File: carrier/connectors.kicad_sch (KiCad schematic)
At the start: 12 parts, among them J1 USB_C_Receptacle_USB2.0, J4 HDMI_D_1.4, J5 USB_C_Receptacle_USB2.0

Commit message: pcb
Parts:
- removed R15: 0, Resistor_SMD:R_0603_1608Metric_Pad0.98x0.95mm_HandSolder, symbol Device:R
- removed R58: 0, Resistor_SMD:R_1210_3225Metric_Pad1.30x2.65mm_HandSolder, symbol Device:R
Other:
- note removed: "Too many people on stack overflow/exchange seem to be unable to agree on this! Leaving this unconnected with a 0 ohm so we can if we choose to - but grounding it could apparently cause a ground loop thingy (which would probably happen since we do not have a true ground in batterys i guess?)"
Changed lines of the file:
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@@
   (junction (at 253.365 46.355) (diameter 0.9144) (color 0 0 0 0))
   (junction (at 271.145 121.92) (diameter 0.9144) (color 0 0 0 0))
-  (junction (at 276.225 72.39) (diameter 0.9144) (color 0 0 0 0))
-  (junction (at 281.94 149.225) (diameter 0.9144) (color 0 0 0 0))
   (no_connect (at 36.83 28.575))
   (no_connect (at 36.83 31.115))
@@
     (stroke (width 0) (type solid) (color 0 0 0 0))
   )
-  (wire (pts (xy 273.685 72.39) (xy 276.225 72.39))
-    (stroke (width 0) (type solid) (color 0 0 0 0))
-  )
   (wire (pts (xy 274.32 28.575) (xy 273.05 28.575))
     (stroke (width 0) (type solid) (color 0 0 0 0))
@@
     (stroke (width 0) (type solid) (color 0 0 0 0))
   )
-  (wire (pts (xy 276.225 64.77) (xy 276.225 72.39))
-    (stroke (width 0) (type solid) (color 0 0 0 0))
-  )
-  (wire (pts (xy 276.225 72.39) (xy 276.225 73.66))
+  (wire (pts (xy 276.225 64.77) (xy 276.225 73.66))
     (stroke (width 0) (type solid) (color 0 0 0 0))
   )
@@
     (stroke (width 0) (type solid) (color 0 0 0 0))
   )
-  (wire (pts (xy 279.4 149.225) (xy 281.94 149.225))
-    (stroke (width 0) (type solid) (color 0 0 0 0))
-  )
-  (wire (pts (xy 281.94 141.605) (xy 281.94 149.225))
-    (stroke (width 0) (type solid) (color 0 0 0 0))
-  )
-  (wire (pts (xy 281.94 149.225) (xy 281.94 150.495))
+  (wire (pts (xy 281.94 141.605) (xy 281.94 150.495))
     (stroke (width 0) (type solid) (color 0 0 0 0))
   )
@@
   (text "NO DATA!" (at 245.745 125.73 0)
     (effects (font (size 1.27 1.27)) (justify left bottom))
-  )
-  (text "Too many people on stack overflow/exchange\nseem to be unable to agree on this! Leaving\nthis unconnected with a 0 ohm so we can if we \nchoose to - but grounding it could apparently \ncause a ground loop thingy (which would probably \nhappen since we do not have a true ground in batterys i guess?)"
-    (at 268.605 81.28 0)
-    (effects (font (size 0.508 0.508)) (justify right bottom))
-  )
-  (text "Too many people on stack overflow/exchange\nseem to be unable to agree on this! Leaving\nthis unconnected with a 0 ohm so we can if we \nchoose to - but grounding it could apparently \ncause a ground loop thingy (which would probably \nhappen since we do not have a true ground in batterys i guess?)"
-    (at 278.13 158.115 0)
-    (effects (font (size 0.508 0.508)) (justify right bottom))
   )
   (text "USB 2.0 Type-C Port (POWER only)\n" (at 282.575 165.1 180)
@@
       (effects (font (size 1.27 1.27)) hide)
     )
-    (pin "1")
-    (pin "2")
-  )
-  (symbol (lib_id "Device:R") (at 269.875 72.39 90) (unit 1)
-    (in_bom yes) (on_board yes)
-    (property "Reference" "R15" (id 0) (at 271.1449 69.85 90)
-      (effects (font (size 1.27 1.27)) (justify left))
-    )
-    (property "Value" "0" (id 1) (at 269.8749 73.025 0)
-      (effects (font (size 1.27 1.27)) (justify left))
-    )
-    (property "Footprint" "Resistor_SMD:R_0603_1608Metric_Pad0.98x0.95mm_HandSolder" (id 2) (at 269.875 74.168 90)
-      (effects (font (size 1.27 1.27)) hide)
-    )
-    (property "Datasheet" "~" (id 3) (at 269.875 72.39 0)
-      (effects (font (size 1.27 1.27)) hide)
-    )
-    (pin "1")
-    (pin "2")
-  )
-  (symbol (lib_id "Device:R") (at 275.59 149.225 90) (unit 1)
-    (in_bom yes) (on_board yes)
-    (property "Reference" "R58" (id 0) (at 275.5899 146.685 90)
-      (effects (font (size 1.27 1.27)) (justify left))
-    )
-    (property "Value" "0" (id 1) (at 275.5899 149.86 0)
-      (effects (font (size 1.27 1.27)) (justify left))
-    )
-    (property "Footprint" "Resistor_SMD:R_1210_3225Metric_Pad1.30x2.65mm_HandSolder" (id 2) (at 275.59 151.003 90)
-      (effects (font (size 1.27 1.27)) hide)
-    )
-    (property "Datasheet" "~" (id 3) (at 275.59 149.225 0)
-      (effects (font (size 1.27 1.27)) hide)
-    )

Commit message: aaaa
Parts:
- added D7: 824011, tvs:SOT95P280X145-5N, symbol tvs:824011
- R56, R57: footprint Resistor_SMD:R_0805_2012Metric_Pad1.20x1.40mm_HandSolder -> Resistor_SMD:R_0603_1608Metric_Pad0.98x0.95mm_HandSolder
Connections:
- net GND: now also R56.2, R57.2, D7.2 (GND); no longer R56.1, R57.1
- net VBUS_CHARGE: now also D7.5 (VDD)
- net at J5.B5 (CC2): now also R56.1; no longer R57.2
- net at J5.A5 (CC1): now also R57.1; no longer R56.2
- net at J5.A6 (D+), J5.B6 (D+): now also D7.3 (I/O1); no longer J5.A7 (D-), J5.B7 (D-)
- new net: D7.4 (I/O2), J5.A7 (D-), J5.B7 (D-)
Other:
- moved on the sheet: R56, R57

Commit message: a
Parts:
- removed R55: 0, Resistor_SMD:R_1210_3225Metric_Pad1.30x2.65mm_HandSolder, symbol Device:R
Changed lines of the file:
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@@
-    (stroke (width 0) (type solid) (color 0 0 0 0))
-  )
-  (wire (pts (xy 198.755 82.55) (xy 198.755 83.185))
-    (stroke (width 0) (type solid) (color 0 0 0 0))
-  )
-  (wire (pts (xy 198.755 83.185) (xy 196.215 83.185))
     (stroke (width 0) (type solid) (color 0 0 0 0))
   )
@@
     (pin "1")
   )
-  (symbol (lib_id "Device:R") (at 198.755 78.74 0) (unit 1)
-    (in_bom yes) (on_board yes)
-    (property "Reference" "R55" (id 0) (at 200.025 78.7399 0)
-      (effects (font (size 1.27 1.27)) (justify left))
-    )
-    (property "Value" "0" (id 1) (at 198.12 78.7399 0)
-      (effects (font (size 1.27 1.27)) (justify left))
-    )
-    (property "Footprint" "Resistor_SMD:R_1210_3225Metric_Pad1.30x2.65mm_HandSolder" (id 2) (at 196.977 78.74 90)
-      (effects (font (size 1.27 1.27)) hide)
-    )
-    (property "Datasheet" "~" (id 3) (at 198.755 78.74 0)
-      (effects (font (size 1.27 1.27)) hide)
-    )
-    (pin "1")
-    (pin "2")
-  )
   (symbol (lib_id "Device:R") (at 227.33 117.475 270) (unit 1)

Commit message: a
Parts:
- removed D6, D7: 824011, tvs:SOT95P280X145-5N, symbol tvs:824011
- added D6, D7: 8240119, CM4IO:SOT143-4L, symbol tvs:8240119
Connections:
- net +5v: now also D7.4 (VDD)
- net GND: now also D6.1 (GND), D7.1 (GND)
- net USB2_D+: now also D7.2 (I/O1)
- net USB2_D-: now also D7.3 (I/O2)
- net VBUS_CHARGE: now also D6.4 (VDD)
- net at J5.A6 (D+), J5.B6 (D+): now also D6.2 (I/O1)
- net at J5.A7 (D-), J5.B7 (D-): now also D6.3 (I/O2)
- no-connect marks 6 -> 5

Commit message: we are nearing completion for this version
maybe one day we will make a second version
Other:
- note added: "Note: probably omit the HDMI connector now,"
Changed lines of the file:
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@@
     (stroke (width 0) (type dash) (color 0 0 0 0))
+  )
+  (text "Note: probably omit the HDMI connector now," (at 129.54 42.672 0)
+    (effects (font (size 1.27 1.27)) (justify left bottom))
   )
   (text "We don't need like, 99% of the pins on this one\nNo PCIe\nNo 2nd HDMI\nNo Camera\nNo DSI/MIPI (For now)"

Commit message: thingy
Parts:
- removed J4: HDMI_D_1.4, Connector_HDMI:HDMI_Micro-D_Molex_46765-1x01, symbol Connector:HDMI_D_1.4
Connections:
- no-connect marks 5 -> 4
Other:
- note added: "UNUSED"
- note removed: "HDMI 1.4 Type-D Port"
- note removed: "Note: probably omit the HDMI connector now,"
- note removed: "TODO: Find out how to do 'differential pairs' in KiCad"

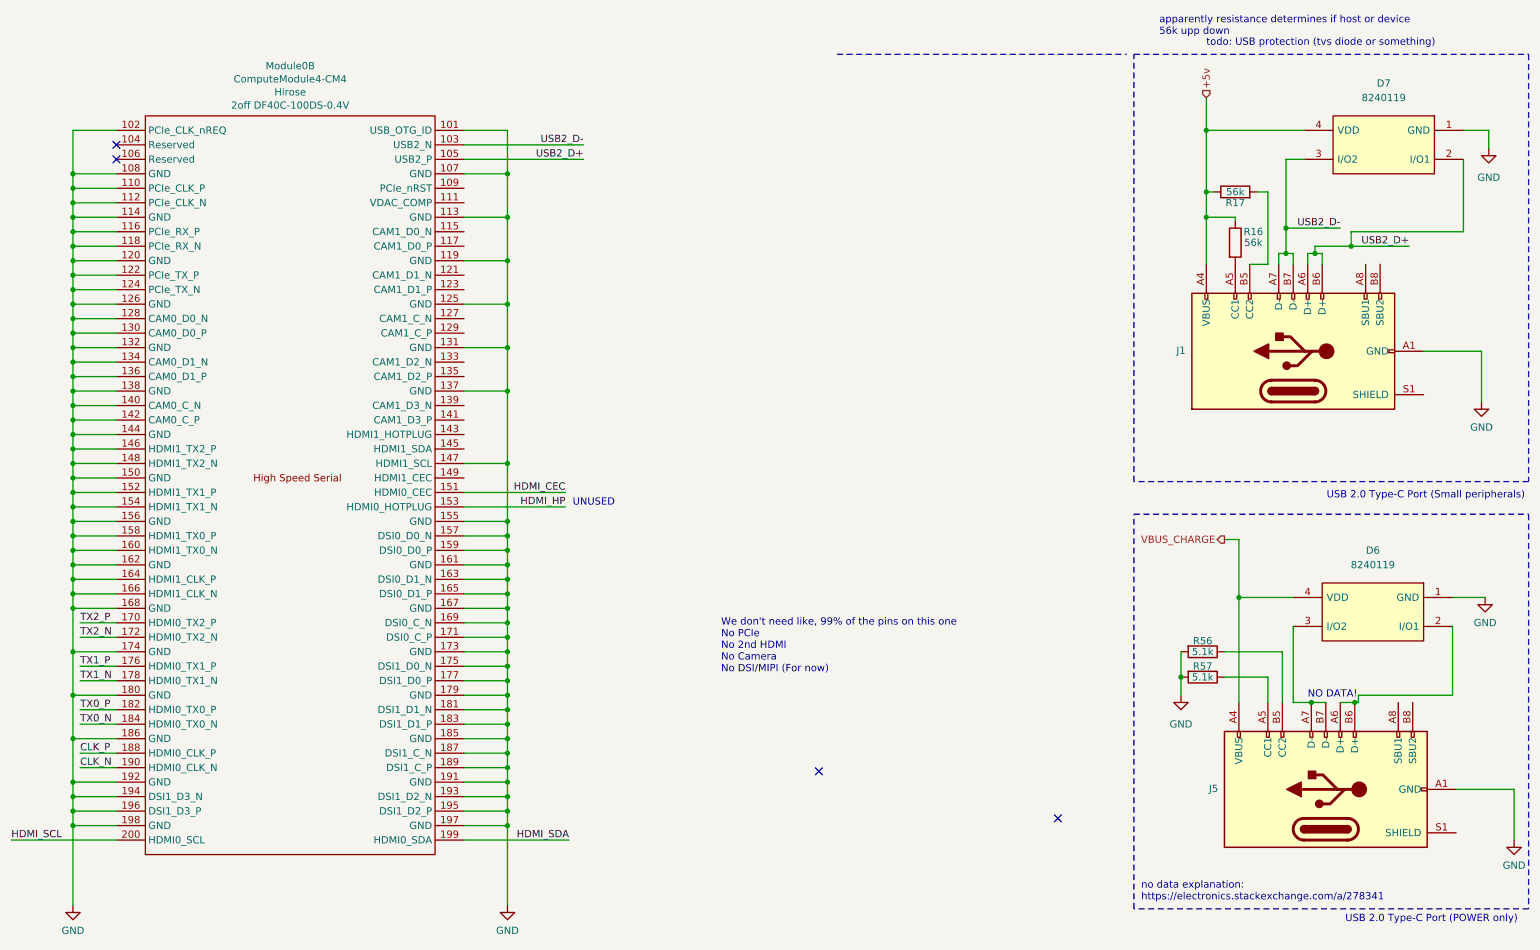
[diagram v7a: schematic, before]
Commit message: fixed switching and added fuel gague
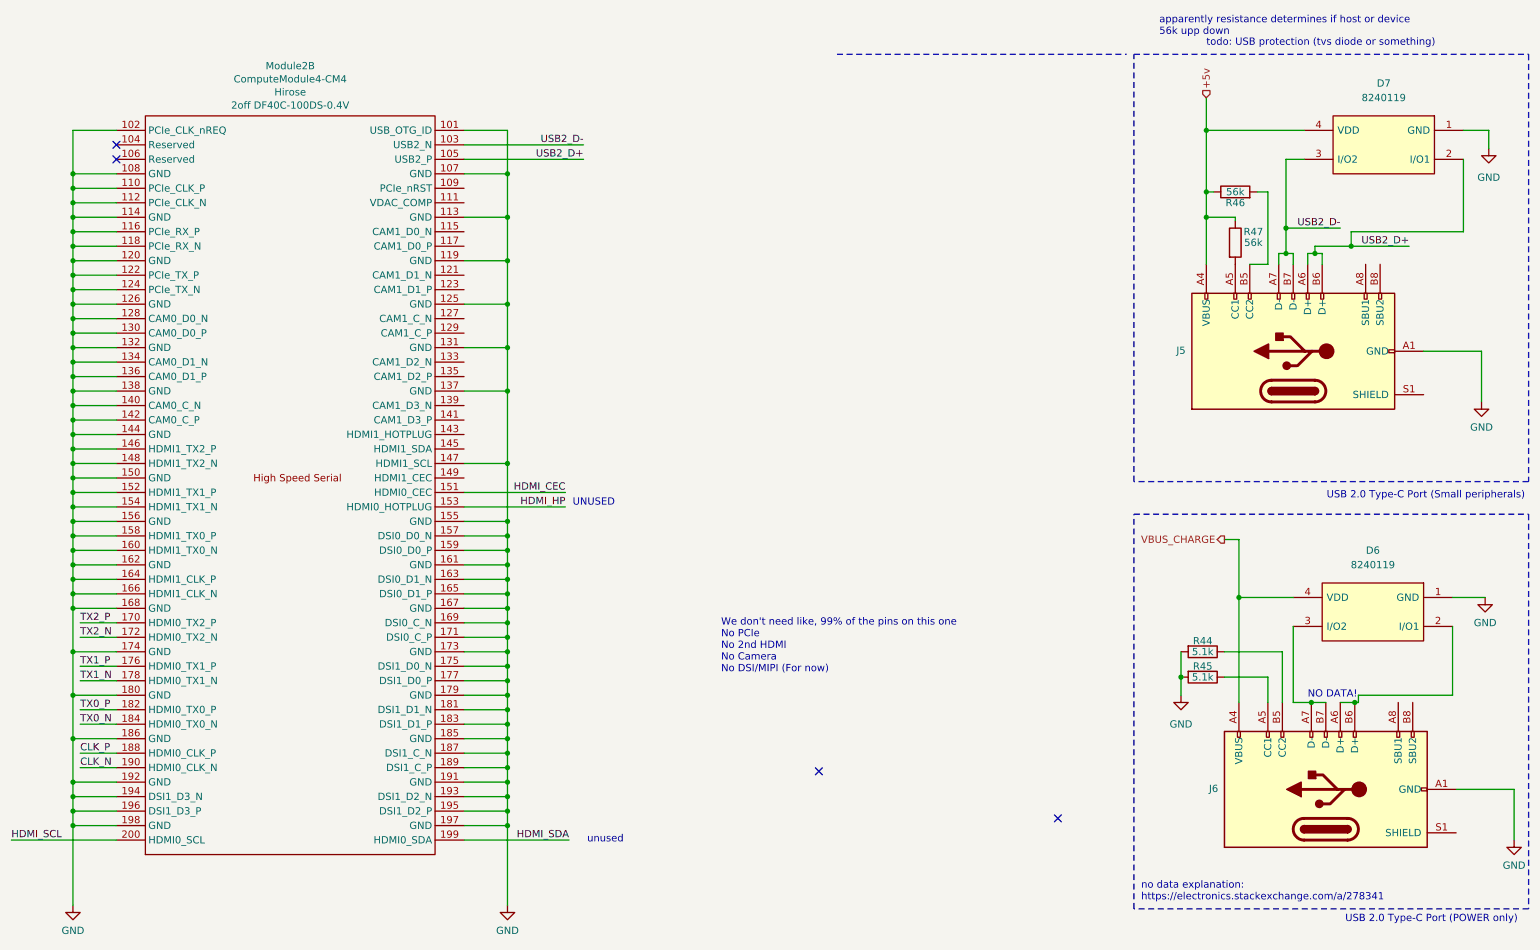
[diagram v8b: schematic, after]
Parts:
- renumbered J1 to J5, J5 to J6, Module0 to Module2, R56 to R44, R57 to R45, R17 to R46, R16 to R47
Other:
- note added: "unused"
